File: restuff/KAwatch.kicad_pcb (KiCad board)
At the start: 2 copper layers, 40 x 51 mm, 24 parts, among them J1 Conn_01x08, J2 USB_C_Receptacle_PowerOnly_6P, J3 Conn_01x02, J4 Conn_01x02, Q1 Q_NPN_BCE, SW1 SW_Push, U1 ESP32-WROOM-32E, U2 MCP73831-2-OT, U3 AMS1117-3.3

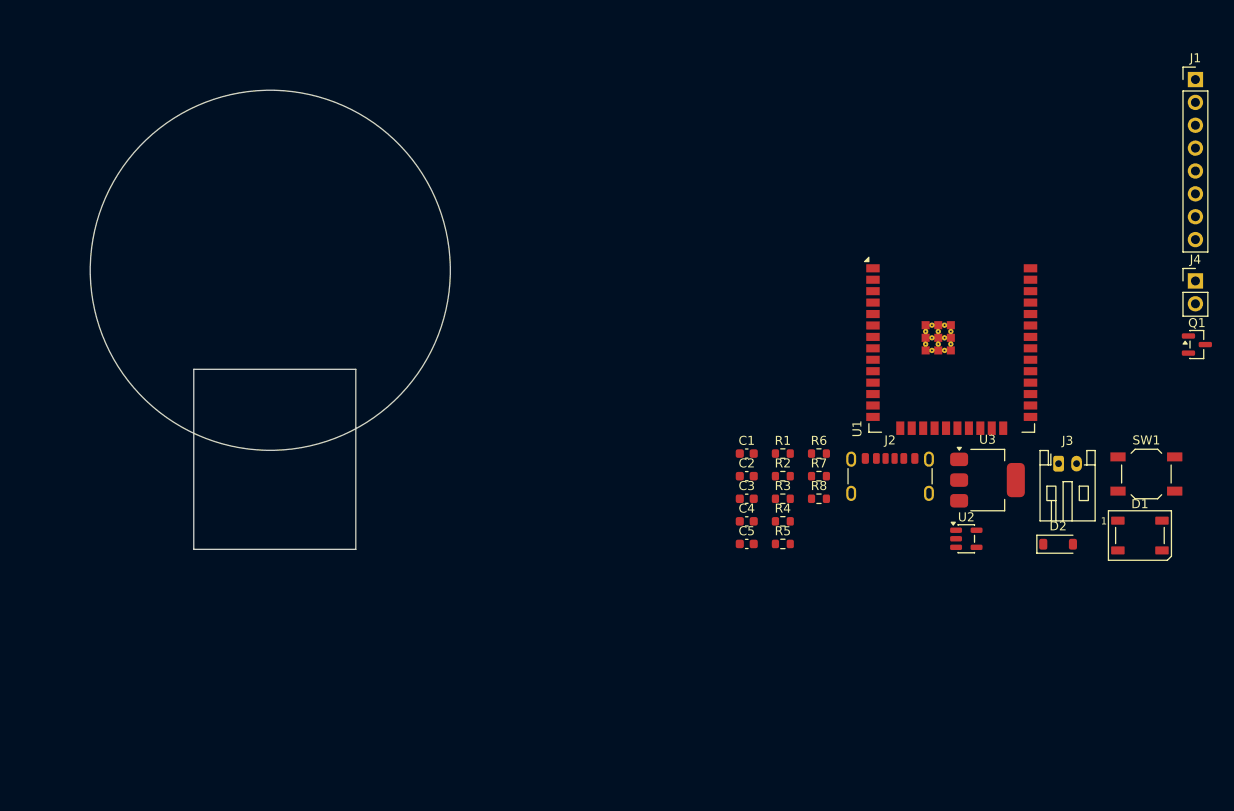
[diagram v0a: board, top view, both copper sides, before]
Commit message: display connector pins updated
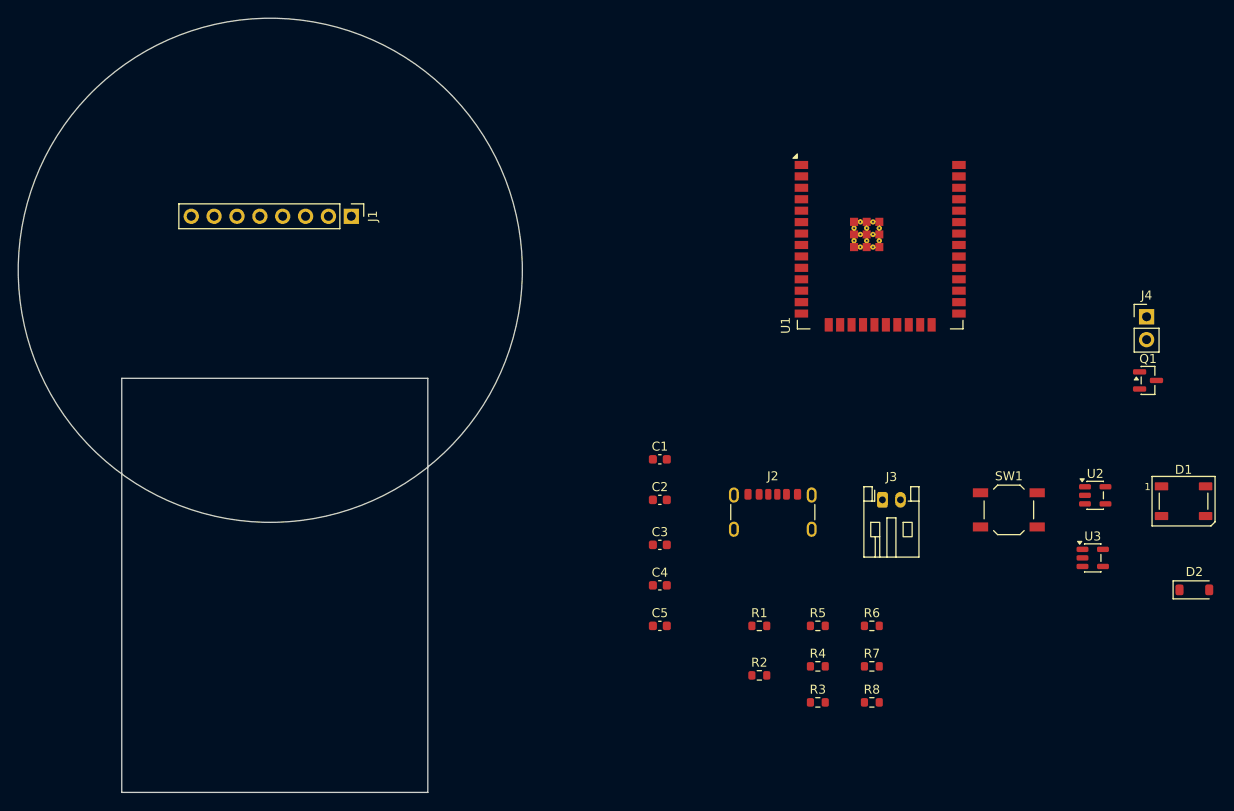
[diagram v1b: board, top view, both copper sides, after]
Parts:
- U3: value AMS1117-3.3 -> XC6220B331MR; footprint Package_TO_SOT_SMD:SOT-223-3_TabPin2 -> Package_TO_SOT_SMD:SOT-23-5
- moved J1 95.0 mm to (127.0, 88.5), turned to -90 degrees
- moved R8 23.4 mm to (184.8, 142.5)
- moved R3 23.0 mm to (178.8, 142.5)
- moved R2 22.3 mm to (172.3, 139.5)
- moved R7 21.9 mm to (184.8, 138.5)
- moved R6 20.0 mm to (184.8, 134.0)
- moved J3 20.0 mm to (186.0, 120.0)
- moved R1 19.3 mm to (172.3, 134.0)
- moved R4 16.6 mm to (178.8, 138.5)
- moved D2 16.0 mm to (220.7, 130.0)
- moved SW1 15.8 mm to (200.0, 121.1)
- moved U2 15.1 mm to (209.6, 119.5)
- moved U3 14.5 mm to (209.4, 126.5)
- moved U1 14.0 mm to (185.8, 88.1)
- moved J2 13.6 mm to (173.8, 122.5)
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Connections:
- J1 pad 1: GND -> /+3V3
- J1 pad 2: /+3V3 -> GND
- J1 pad 3: /<NO NET> -> /DISP_MOSI
- J1 pad 4: /DISP_MOSI -> /DISP_SCK
- J1 pad 5: /DISP_RST -> /DISP_CS
- J1 pad 7: /DISP_CS -> /DISP_RST
- U1 pad 30: /<NO NET> -> /DISP_SCK
- U3 pad 1: GND -> Net-(J3-BAT+)
- U3 pad 2: /+3V3 -> GND
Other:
- board size 40 x 51 mm -> 56 x 86 mm

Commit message: mcu and display add to pcb
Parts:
- moved U1 83.9 mm to (118.5, 138.2), turned to 180 degrees
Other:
- board size 56 x 86 mm -> 56 x 78 mm

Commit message: pcb mods
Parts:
- moved U2 105.6 mm to (104.0, 120.0)
- moved J3 83.7 mm to (104.5, 139.0)
- moved U3 78.1 mm to (132.0, 137.0)
- moved R4 75.1 mm to (104.0, 132.0)
- moved C1 61.2 mm to (101.0, 126.0)
- moved C2 54.6 mm to (107.0, 126.0)
- moved R3 49.7 mm to (131.0, 129.0)
- moved R2 43.8 mm to (131.0, 125.0)
- moved J2 39.1 mm to (135.0, 118.0)
- moved C3 34.4 mm to (129.0, 137.0)
- moved C4 27.3 mm to (135.0, 137.0)
- moved U1 8.37 mm to (118.5, 129.8)
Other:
- outline, holes or cut-outs redrawn
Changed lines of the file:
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@@
 	(footprint "Capacitor_SMD:C_0603_1608Metric"
 		(layer "F.Cu")
-		(at 161.275 120)
+		(at 107 126)
 		(descr "Capacitor SMD 0603 (1608 Metric), square (rectangular) end terminal, IPC-7351 nominal, (Body size source: IPC-SM-782 page 76, https://www.pcb-3d.com/wordpress/wp-content/uploads/ipc-sm-782a_amendment_1_and_2.pdf)")
 		(tags "capacitor")
@@
 	(footprint "RF_Module:ESP32-WROOM-32E"
 		(layer "F.Cu")
-		(at 118.5 138.17 180)
+		(at 118.5 129.8 180)
 		(descr "2.4 GHz Wi­-Fi and Bluetooth 5 (LE) module: https://www.espressif.com/sites/default/files/documentation/esp32-wroom-32e_esp32-wroom-32ue_datasheet_en.pdf")
 		(tags "Bluetooth WiFi Wi-Fi ESP32 WROOM Xtensa LX6")
@@
 			(polygon
 				(pts
-					(xy 142.5 165.92) (xy 94.5 165.92) (xy 94.5 144.73) (xy 142.5 144.73)
+					(xy 142.5 157.55) (xy 94.5 157.55) (xy 94.5 136.36) (xy 142.5 136.36)
 				)
 			)
@@
 	(footprint "Package_TO_SOT_SMD:SOT-23-5"
 		(layer "F.Cu")
-		(at 209.3625 126.45)
+		(at 132 137)
 		(descr "SOT, 5 Pin (JEDEC MO-178 Var AA https://www.jedec.org/document_search?search_api_views_fulltext=MO-178)")
 		(tags "SOT TO_SOT_SMD")
@@
 	(footprint "Capacitor_SMD:C_0603_1608Metric"
 		(layer "F.Cu")
-		(at 161.275 115.5)
+		(at 101 126)
 		(descr "Capacitor SMD 0603 (1608 Metric), square (rectangular) end terminal, IPC-7351 nominal, (Body size source: IPC-SM-782 page 76, https://www.pcb-3d.com/wordpress/wp-content/uploads/ipc-sm-782a_amendment_1_and_2.pdf)")
 		(tags "capacitor")
@@
 	(footprint "Capacitor_SMD:C_0603_1608Metric"
 		(layer "F.Cu")
-		(at 161.275 129.5)
+		(at 135 137)
 		(descr "Capacitor SMD 0603 (1608 Metric), square (rectangular) end terminal, IPC-7351 nominal, (Body size source: IPC-SM-782 page 76, https://www.pcb-3d.com/wordpress/wp-content/uploads/ipc-sm-782a_amendment_1_and_2.pdf)")
 		(tags "capacitor")
@@
 	(footprint "Package_TO_SOT_SMD:SOT-23-5"
 		(layer "F.Cu")
-		(at 209.6375 119.5)
+		(at 104 120)
 		(descr "SOT, 5 Pin (JEDEC MO-178 Var AA https://www.jedec.org/document_search?search_api_views_fulltext=MO-178)")
 		(tags "SOT TO_SOT_SMD")
@@
 	(footprint "Connector_JST:JST_PH_S2B-PH-K_1x02_P2.00mm_Horizontal"
 		(layer "F.Cu")
-		(at 186 120)
+		(at 104.5 139)
 		(descr "JST PH series connector, S2B-PH-K (http://www.jst-mfg.com/product/pdf/eng/ePH.pdf)")
 		(tags "connector JST PH horizontal")
@@
 	(footprint "Resistor_SMD:R_0603_1608Metric"
 		(layer "F.Cu")
-		(at 178.825 138.5)
+		(at 104 132)
 		(descr "Resistor SMD 0603 (1608 Metric), square (rectangular) end terminal, IPC-7351 nominal, (Body size source: IPC-SM-782 page 72, https://www.pcb-3d.com/wordpress/wp-content/uploads/ipc-sm-782a_amendment_1_and_2.pdf)")
 		(tags "resistor")
@@
 	(footprint "Connector_USB:USB_C_Receptacle_GCT_USB4125-xx-x_6P_TopMnt_Horizontal"
 		(layer "F.Cu")
-		(at 173.82 122.465)
+		(at 135 118)
 		(descr "USB Type C Receptacle, GCT, power-only, 6P, top mounted, horizontal, 3A, 1mm stake: https://gct.co/files/drawings/usb4125.pdf")
 		(tags "USB C Type-C receptacle power-only charging-only 6P 6C right angled")
@@
 	(footprint "Capacitor_SMD:C_0603_1608Metric"
 		(layer "F.Cu")
-		(at 161.275 125)
+		(at 129 137)
 		(descr "Capacitor SMD 0603 (1608 Metric), square (rectangular) end terminal, IPC-7351 nominal, (Body size source: IPC-SM-782 page 76, https://www.pcb-3d.com/wordpress/wp-content/uploads/ipc-sm-782a_amendment_1_and_2.pdf)")
 		(tags "capacitor")
@@
 	(footprint "Resistor_SMD:R_0603_1608Metric"
 		(layer "F.Cu")
-		(at 172.325 139.5)
+		(at 131 125)
 		(descr "Resistor SMD 0603 (1608 Metric), square (rectangular) end terminal, IPC-7351 nominal, (Body size source: IPC-SM-782 page 72, https://www.pcb-3d.com/wordpress/wp-content/uploads/ipc-sm-782a_amendment_1_and_2.pdf)")
 		(tags "resistor")
@@
 	(footprint "Resistor_SMD:R_0603_1608Metric"
 		(layer "F.Cu")
-		(at 178.825 142.5)
+		(at 131 129)
 		(descr "Resistor SMD 0603 (1608 Metric), square (rectangular) end terminal, IPC-7351 nominal, (Body size source: IPC-SM-782 page 72, https://www.pcb-3d.com/wordpress/wp-content/uploads/ipc-sm-782a_amendment_1_and_2.pdf)")
 		(tags "resistor")
@@
 		(layer "Cmts.User")
 	)
-	(gr_rect
-		(start 99.5 106.5)
+	(gr_line
+		(start 99.5 115.07)
+		(end 99.5 144.5)
+		(stroke
+			(width 0.05)
+			(type solid)
+		)
+		(layer "Edge.Cuts")
+	)
+	(gr_arc
+		(start 99.5 115.07)
+		(mid 118.5 66.5)
+		(end 137.5 115.07)
+		(stroke
+			(width 0.05)
+			(type solid)
+		)
+		(layer "Edge.Cuts")
+	)
+	(gr_line
+		(start 99.5 144.5)
 		(end 137.5 144.5)
 		(stroke
@@
 			(type solid)
 		)
-		(fill no)
 		(layer "Edge.Cuts")
 	)
-	(gr_circle
-		(center 118.5 94.5)
-		(end 146.5 94.5)
+	(gr_line
+		(start 137.5 144.5)
+		(end 137.5 115.07)
 		(stroke
 			(width 0.05)
 			(type solid)
 		)
-		(fill no)
 		(layer "Edge.Cuts")
 	)

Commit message: compacting pcb
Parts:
- moved J3 7.83 mm to (101.0, 132.0), turned to 90 degrees
- moved R4 7.28 mm to (106.0, 125.0)
- moved U3 7.08 mm to (131.3, 129.9)
- moved R3 4.37 mm to (134.2, 126.0)
- moved C3 4.34 mm to (130.7, 133.0)
- moved C1 4.27 mm to (102.5, 122.0)
- moved C4 4.14 mm to (133.9, 133.0)
- moved C2 4.12 mm to (106.0, 122.0)
- moved U2 2.46 mm to (105.4, 118.0)
- moved J2 2.07 mm to (133.6, 119.5), turned to 90 degrees
- moved U1 1.63 mm to (118.5, 128.2)
- moved R2 1.05 mm to (130.7, 126.0)
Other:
- board size 56 x 78 mm -> 56 x 74.5 mm

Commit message: pcb edits and routing start
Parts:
- moved D1 125.1 mm to (101.5, 78.7)
- moved SW1 97.5 mm to (103.2, 109.9)
- moved D2 86.5 mm to (136.0, 112.0)
- moved J4 84.9 mm to (131.0, 109.0)
- moved R8 79.3 mm to (136.0, 80.0)
- moved Q1 76.5 mm to (139.0, 109.0)
- moved R5 70.2 mm to (111.8, 113.0)
- moved R1 67.6 mm to (136.0, 77.0)
- moved R6 63.6 mm to (124.8, 113.0)
- moved R7 58.6 mm to (134.8, 108.0)
- moved C5 47.9 mm to (118.3, 113.0)
- moved R3 2.00 mm to (136.2, 126.0)
- moved J3 1.00 mm to (101.0, 131.0)
- moved U1 0.17 mm to (118.5, 128.0)
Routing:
- net /+3V3: track 0.00 -> 39.0 mm
- net GND: track 0.00 -> 32.0 mm
- net Net-(U1-IO0): track 0.00 -> 24.8 mm
- net Net-(U1-IO14): track 0.00 -> 17.9 mm
- net Net-(D2-A): track 0.00 -> 12.2 mm
- net Net-(U1-IO34): track 0.00 -> 3.68 mm
- net Net-(Q1-B): track 0.00 -> 2.43 mm

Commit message: routing
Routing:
- net GND: track 32.0 -> 87.4 mm
- net Net-(U1-IO13): track 0.00 -> 38.6 mm
- net /+3V3: track 39.0 -> 76.4 mm
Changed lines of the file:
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@@
+	)
+	(segment
+		(start 100.5 75.5)
+		(end 133.675 75.5)
+		(width 0.2)
+		(layer "F.Cu")
+		(net "/+3V3")
 	)
 	(segment
@@
 	)
 	(segment
+		(start 99 77)
+		(end 100.5 75.5)
+		(width 0.2)
+		(layer "F.Cu")
+		(net "/+3V3")
+	)
+	(segment
 		(start 133.5 112)
 		(end 133 111.5)
@@
 	)
 	(segment
+		(start 133.675 75.5)
+		(end 135.175 77)
+		(width 0.2)
+		(layer "F.Cu")
+		(net "/+3V3")
+	)
+	(segment
 		(start 124 113)
 		(end 123.225 112.225)
@@
 	)
 	(segment
+		(start 135.5 114)
+		(end 135.5 114.06)
+		(width 0.2)
+		(layer "F.Cu")
+		(net "GND")
+	)
+	(segment
+		(start 139.9375 112.9375)
+		(end 140 113)
+		(width 0.2)
+		(layer "F.Cu")
+		(net "GND")
+	)
+	(segment
+		(start 139 114)
+		(end 135.5 114)
+		(width 0.2)
+		(layer "F.Cu")
+		(net "GND")
+	)
+	(segment
+		(start 140 113)
+		(end 139 114)
+		(width 0.2)
+		(layer "F.Cu")
+		(net "GND")
+	)
+	(segment
+		(start 100 117)
+		(end 100.95 117.95)
+		(width 0.2)
+		(layer "F.Cu")
+		(net "GND")
+	)
+	(segment
 		(start 136.825 80)
 		(end 136.825 90.175)
@@
 	)
 	(segment
+		(start 100 111.8)
+		(end 100 111.5)
+		(width 0.2)
+		(layer "F.Cu")
+		(net "GND")
+	)
+	(segment
 		(start 125 91)
 		(end 124.46 90.46)
@@
 	)
 	(segment
+		(start 100 111.8)
+		(end 106.3 111.8)
+		(width 0.2)
+		(layer "F.Cu")
+		(net "GND")
+	)
+	(segment
 		(start 136 91)
 		(end 125 91)
@@
 	)
 	(segment
+		(start 100.95 117.95)
+		(end 104.225 117.95)
+		(width 0.2)
+		(layer "F.Cu")
+		(net "GND")
+	)
+	(segment
+		(start 135.5 114.06)
+		(end 134.38 115.18)
+		(width 0.2)
+		(layer "F.Cu")
+		(net "GND")
+	)
+	(segment
+		(start 139.9375 109)
+		(end 139.9375 112.9375)
+		(width 0.2)
+		(layer "F.Cu")
+		(net "GND")
+	)
+	(segment
 		(start 124.46 90.46)
 		(end 124.46 88.5)
@@
 	)
 	(segment
+		(start 124.46 80.96)
+		(end 124.46 88.5)
+		(width 0.2)
+		(layer "F.Cu")
+		(net "GND")
+	)
+	(segment
+		(start 103.9 80.3)
+		(end 123.8 80.3)
+		(width 0.2)
+		(layer "F.Cu")
+		(net "GND")
+	)
+	(segment
 		(start 122.665 113)
 		(end 124.215 114.55)
@@
 	)
 	(segment
+		(start 100 111.8)
+		(end 100 117)
+		(width 0.2)
+		(layer "F.Cu")
+		(net "GND")
+	)
+	(segment
 		(start 124.215 114.55)
 		(end 124.215 115.5)
@@
 	)
 	(segment
+		(start 123.8 80.3)
+		(end 124.46 80.96)
+		(width 0.2)
+		(layer "F.Cu")
+		(net "GND")
+	)
+	(segment
 		(start 136.825 80)
 		(end 137 80)
@@
 	)
 	(segment
+		(start 124.5 108)
+		(end 127 110.5)
+		(width 0.2)
+		(layer "F.Cu")
+		(net "Net-(U1-IO13)")
+	)
+	(segment
+		(start 123.495 117)
+		(end 122.945 116.45)
+		(width 0.2)
+		(layer "F.Cu")
+		(net "Net-(U1-IO13)")
+	)
+	(segment
+		(start 127 115)
+		(end 125 117)
+		(width 0.2)
+		(layer "F.Cu")
+		(net "Net-(U1-IO13)")
+	)
+	(segment
+		(start 122.945 116.45)
+		(end 122.945 115.5)
+		(width 0.2)
+		(layer "F.Cu")
+		(net "Net-(U1-IO13)")
+	)
+	(segment
+		(start 127 110.5)
+		(end 127 115)
+		(width 0.2)
+		(layer "F.Cu")
+		(net "Net-(U1-IO13)")
+	)
+	(segment
+		(start 100 108)
+		(end 106.3 108)
+		(width 0.2)
+		(layer "F.Cu")
+		(net "Net-(U1-IO13)")
+	)
+	(segment
+		(start 106.3 108)
+		(end 124.5 108)
+		(width 0.2)
+		(layer "F.Cu")
+		(net "Net-(U1-IO13)")
+	)
+	(segment
+		(start 125 117)
+		(end 123.495 117)
+		(width 0.2)
+		(layer "F.Cu")
+		(net "Net-(U1-IO13)")
+	)
+	(segment
